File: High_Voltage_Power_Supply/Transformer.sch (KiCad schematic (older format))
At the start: 6 parts

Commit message: Finalised the schematic and BOM
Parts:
- TR1, TR2, TR3, TR4, TR5, TR6: renamed from TR?; Link (none) -> https://www.mouser.com/ProductDetail/Coilcraft/GA3460-BL?qs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
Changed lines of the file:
@@
 	3500 1800 3500 1700
 $Comp
-L High_Voltage_Power_Supply:GA3460-BL TR?
+L High_Voltage_Power_Supply:GA3460-BL TR1
 U 1 1 5F60E716
 P 4100 2000
-F 0 "TR?" H 4057 1285 50  0000 C CNN
+F 0 "TR1" H 4057 1285 50  0000 C CNN
 F 1 "GA3460-BL" H 4057 1376 50  0000 C CNN
 F 2 "High_Voltage_Power_Supply:Transformer_Coilcraft_GA3460-BL" H 4150 1300 50  0001 C CNN
-F 3 "" H 4000 2000 50  0001 C CNN
+F 3 "https://www.mouser.com/datasheet/2/597/ga3459-463457.pdf" H 4000 2000 50  0001 C CNN
+F 4 "https://www.mouser.com/ProductDetail/Coilcraft/GA3460-BL?qs=ZYnrCdKdyeeqpRItZMyzHA%3D%3D" H 4100 2000 50  0001 C CNN "Link"
 	1    4100 2000
 	1    0    0    1
 $EndComp
 $Comp
-L High_Voltage_Power_Supply:GA3460-BL TR?
+L High_Voltage_Power_Supply:GA3460-BL TR2
 U 1 1 5F683ED0
 P 6600 2000
-F 0 "TR?" H 6557 1285 50  0000 C CNN
+F 0 "TR2" H 6557 1285 50  0000 C CNN
 F 1 "GA3460-BL" H 6557 1376 50  0000 C CNN
 F 2 "High_Voltage_Power_Supply:Transformer_Coilcraft_GA3460-BL" H 6650 1300 50  0001 C CNN
-F 3 "" H 6500 2000 50  0001 C CNN
+F 3 "https://www.mouser.com/datasheet/2/597/ga3459-463457.pdf" H 6500 2000 50  0001 C CNN
+F 4 "https://www.mouser.com/ProductDetail/Coilcraft/GA3460-BL?qs=ZYnrCdKdyeeqpRItZMyzHA%3D%3D" H 6600 2000 50  0001 C CNN "Link"
 	1    6600 2000
 	1    0    0    1
@@
 	6000 2500 6000 2600
 $Comp
-L High_Voltage_Power_Supply:GA3460-BL TR?
+L High_Voltage_Power_Supply:GA3460-BL TR3
 U 1 1 5F68609E
 P 4100 3500
-F 0 "TR?" H 4057 2785 50  0000 C CNN
+F 0 "TR3" H 4057 2785 50  0000 C CNN
 F 1 "GA3460-BL" H 4057 2876 50  0000 C CNN
 F 2 "High_Voltage_Power_Supply:Transformer_Coilcraft_GA3460-BL" H 4150 2800 50  0001 C CNN
-F 3 "" H 4000 3500 50  0001 C CNN
+F 3 "https://www.mouser.com/datasheet/2/597/ga3459-463457.pdf" H 4000 3500 50  0001 C CNN
+F 4 "https://www.mouser.com/ProductDetail/Coilcraft/GA3460-BL?qs=ZYnrCdKdyeeqpRItZMyzHA%3D%3D" H 4100 3500 50  0001 C CNN "Link"
 	1    4100 3500
 	1    0    0    1
@@
 	3500 4000 3500 4100
 $Comp
-L High_Voltage_Power_Supply:GA3460-BL TR?
+L High_Voltage_Power_Supply:GA3460-BL TR4
 U 1 1 5F6896C3
 P 6600 3500
-F 0 "TR?" H 6557 2785 50  0000 C CNN
+F 0 "TR4" H 6557 2785 50  0000 C CNN
 F 1 "GA3460-BL" H 6557 2876 50  0000 C CNN
 F 2 "High_Voltage_Power_Supply:Transformer_Coilcraft_GA3460-BL" H 6650 2800 50  0001 C CNN
-F 3 "" H 6500 3500 50  0001 C CNN
+F 3 "https://www.mouser.com/datasheet/2/597/ga3459-463457.pdf" H 6500 3500 50  0001 C CNN
+F 4 "https://www.mouser.com/ProductDetail/Coilcraft/GA3460-BL?qs=ZYnrCdKdyeeqpRItZMyzHA%3D%3D" H 6600 3500 50  0001 C CNN "Link"
 	1    6600 3500
 	1    0    0    1
@@
 	6000 4000 6000 4100
 $Comp
-L High_Voltage_Power_Supply:GA3460-BL TR?
+L High_Voltage_Power_Supply:GA3460-BL TR6
 U 1 1 5F68DCC8
 P 6600 5000
-F 0 "TR?" H 6557 4285 50  0000 C CNN
+F 0 "TR6" H 6557 4285 50  0000 C CNN
 F 1 "GA3460-BL" H 6557 4376 50  0000 C CNN
 F 2 "High_Voltage_Power_Supply:Transformer_Coilcraft_GA3460-BL" H 6650 4300 50  0001 C CNN
-F 3 "" H 6500 5000 50  0001 C CNN
+F 3 "https://www.mouser.com/datasheet/2/597/ga3459-463457.pdf" H 6500 5000 50  0001 C CNN
+F 4 "https://www.mouser.com/ProductDetail/Coilcraft/GA3460-BL?qs=ZYnrCdKdyeeqpRItZMyzHA%3D%3D" H 6600 5000 50  0001 C CNN "Link"
 	1    6600 5000
 	1    0    0    1
 $EndComp
 $Comp
-L High_Voltage_Power_Supply:GA3460-BL TR?
+L High_Voltage_Power_Supply:GA3460-BL TR5
 U 1 1 5F69028C
 P 4100 5000
-F 0 "TR?" H 4057 4285 50  0000 C CNN
+F 0 "TR5" H 4057 4285 50  0000 C CNN
 F 1 "GA3460-BL" H 4057 4376 50  0000 C CNN
 F 2 "High_Voltage_Power_Supply:Transformer_Coilcraft_GA3460-BL" H 4150 4300 50  0001 C CNN
-F 3 "" H 4000 5000 50  0001 C CNN
+F 3 "https://www.mouser.com/datasheet/2/597/ga3459-463457.pdf" H 4000 5000 50  0001 C CNN
+F 4 "https://www.mouser.com/ProductDetail/Coilcraft/GA3460-BL?qs=ZYnrCdKdyeeqpRItZMyzHA%3D%3D" H 4100 5000 50  0001 C CNN "Link"
 	1    4100 5000
 	1    0    0    1

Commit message: Finished most of the PCB layout
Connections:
- net in+: now also TR2.1, TR2.2, TR2.3, TR2.4; no longer TR2.10, TR2.11, TR2.12, TR2.9
- net in-: now also TR6.10, TR6.11, TR6.12, TR6.9; no longer TR6.1, TR6.2, TR6.3, TR6.4
- net out+: now also TR2.6; no longer TR2.7
- net out-: now also TR6.7; no longer TR6.6
- net at TR1.1, TR1.2, TR1.3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: now also TR2.10, TR2.11, TR2.12, TR2.9, TR4.1, TR4.2, TR4.3, TR4.4; no longer TR2.1, TR2.2, TR2.3, TR2.4, TR4.10, TR4.11, TR4.12, TR4.9
- net at TR1.6, TR3.7: now also TR2.7, TR4.6; no longer TR2.6, TR4.7
- net at TR3.1, TR3.2, TR3.3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: now also TR4.10, TR4.11, TR4.12, TR4.9, TR6.1, TR6.2, TR6.3, TR6.4; no longer TR4.1, TR4.2, TR4.3, TR4.4, TR6.10, TR6.11, TR6.12, TR6.9
- net at TR3.6, TR5.7: now also TR4.7, TR6.6; no longer TR4.6, TR6.7
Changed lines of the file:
@@
 F 4 "https://www.mouser.com/ProductDetail/Coilcraft/GA3460-BL?qs=ZYnrCdKdyeeqpRItZMyzHA%3D%3D" H 6600 2000 50  0001 C CNN "Link"
 	1    6600 2000
-	1    0    0    1
+	1    0    0    -1
 $EndComp
 Wire Wire Line
@@
 F 4 "https://www.mouser.com/ProductDetail/Coilcraft/GA3460-BL?qs=ZYnrCdKdyeeqpRItZMyzHA%3D%3D" H 6600 3500 50  0001 C CNN "Link"
 	1    6600 3500
-	1    0    0    1
+	1    0    0    -1
 $EndComp
 Wire Wire Line
@@
 F 4 "https://www.mouser.com/ProductDetail/Coilcraft/GA3460-BL?qs=ZYnrCdKdyeeqpRItZMyzHA%3D%3D" H 6600 5000 50  0001 C CNN "Link"
 	1    6600 5000
-	1    0    0    1
+	1    0    0    -1
 $EndComp
 $Comp

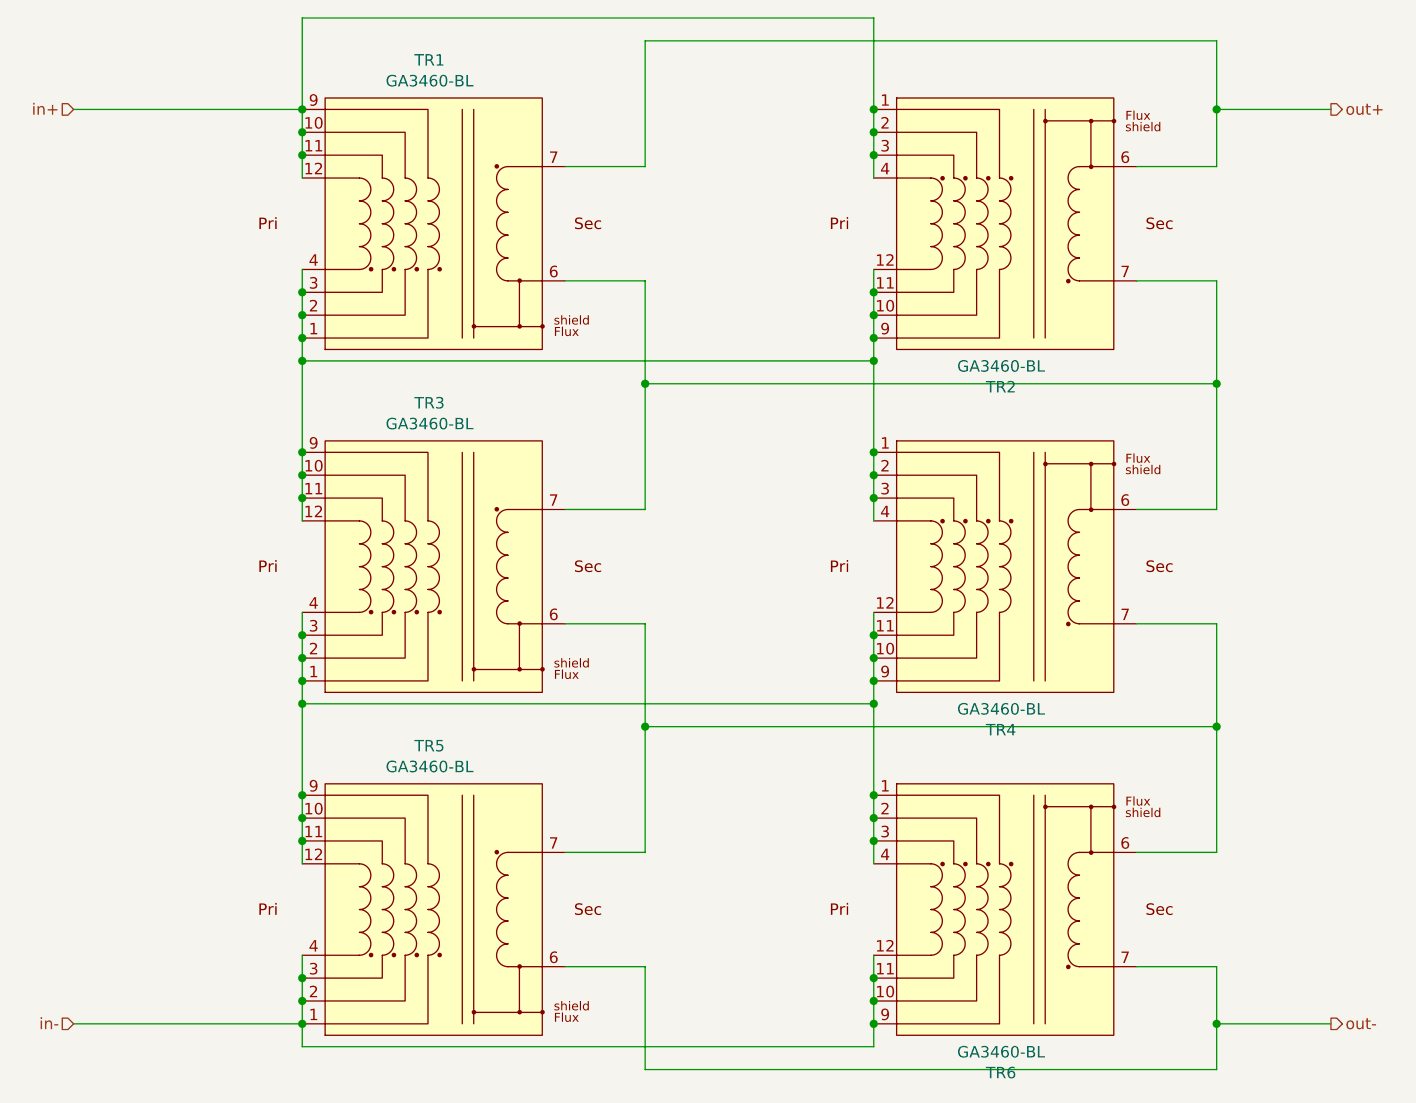
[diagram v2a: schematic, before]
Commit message: Updated schematic to run on regulation mode only
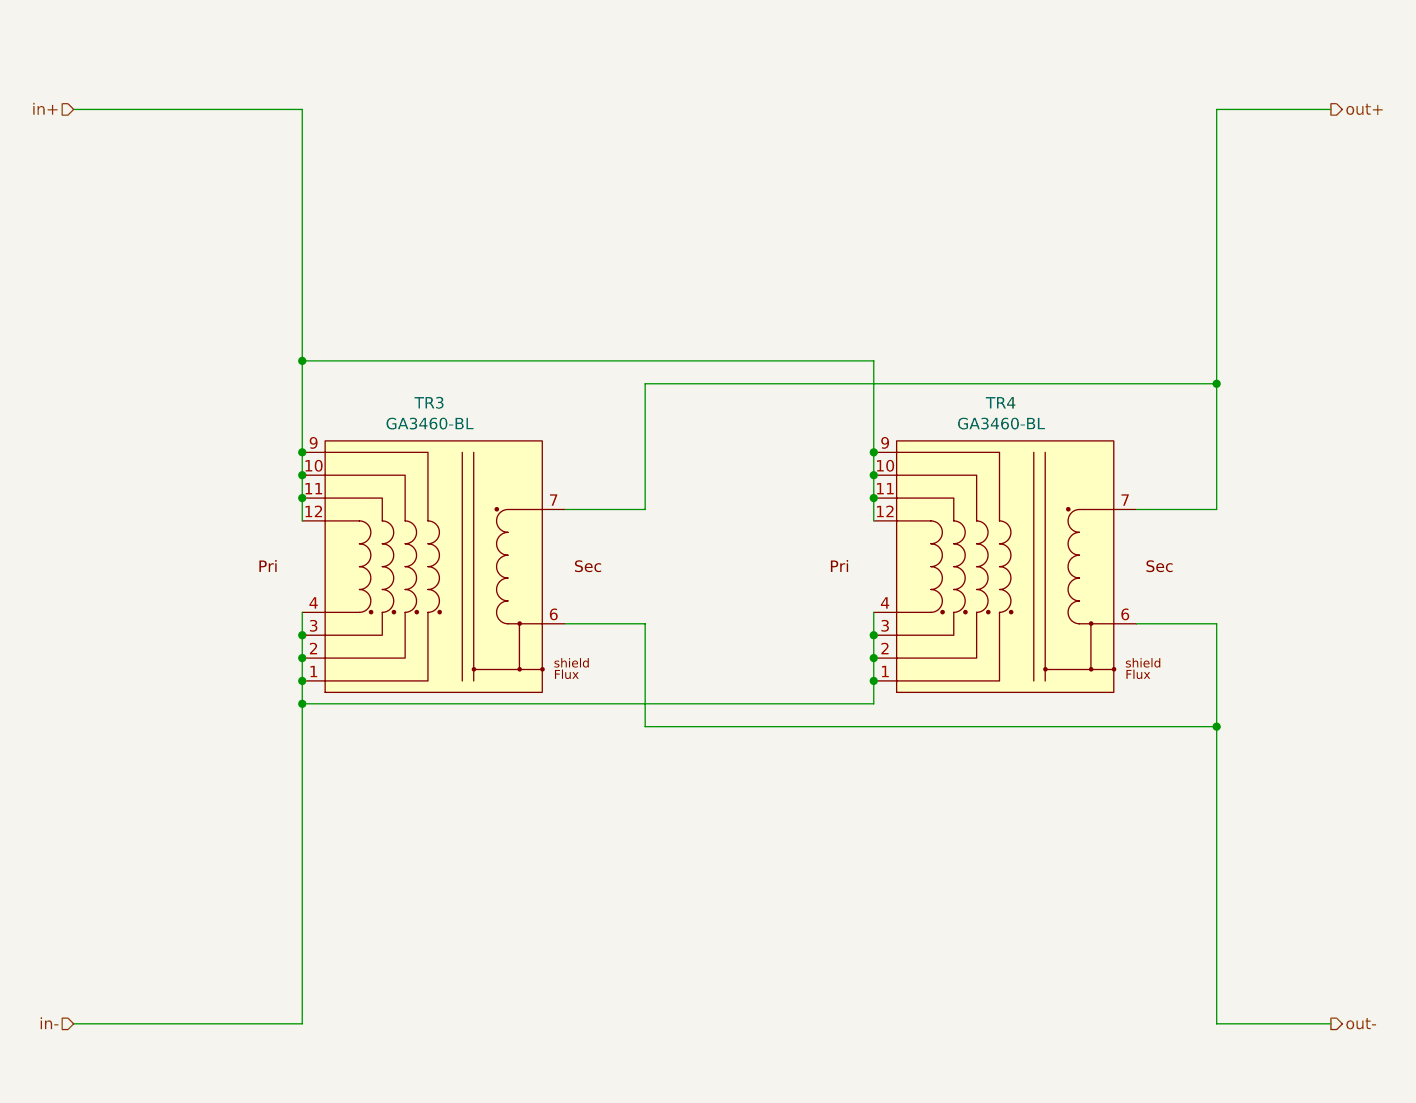
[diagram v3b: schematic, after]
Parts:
- removed TR1, TR2, TR5, TR6: GA3460-BL, High_Voltage_Power_Supply:Transformer_Coilcraft_GA3460-BL, symbol High_Voltage_Power_Supply:GA3460-BL
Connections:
- net in+: now also TR3.10, TR3.11, TR3.12, TR3.9, TR4.10, TR4.11, TR4.12, TR4.9
- net in-: now also TR3.1, TR3.2, TR3.3, TR3.4, TR4.1, TR4.2, TR4.3, TR4.4
- net out+: now also TR3.7, TR4.7
- net out-: now also TR3.6, TR4.6
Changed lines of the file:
@@
 	2500 5500 3500 5500
 Wire Wire Line
-	3500 2600 6000 2600
-Wire Wire Line
 	3500 4100 6000 4100
-Connection ~ 6000 4100
-Connection ~ 3500 4100
-Connection ~ 3500 2600
-Connection ~ 6000 2600
 Wire Wire Line
 	2500 1500 3500 1500
-Connection ~ 3500 1500
 Wire Wire Line
 	4650 3250 5000 3250
@@
 	5000 3250 5000 2700
 Wire Wire Line
-	4650 4750 5000 4750
-Wire Wire Line
-	5000 4750 5000 4200
-Wire Wire Line
 	4650 3750 5000 3750
 Wire Wire Line
 	5000 3750 5000 4200
-Connection ~ 5000 4200
-Wire Wire Line
-	4650 2250 5000 2250
-Wire Wire Line
-	5000 2250 5000 2700
-Connection ~ 5000 2700
-Wire Wire Line
-	4650 1750 5000 1750
-Wire Wire Line
-	5000 1750 5000 1200
-Wire Wire Line
-	5000 1200 7500 1200
-Wire Wire Line
-	7150 1750 7500 1750
-Wire Wire Line
-	7500 1750 7500 1500
 Wire Wire Line
 	7500 3250 7500 2700
 Wire Wire Line
-	7500 2250 7150 2250
-Wire Wire Line
 	5000 2700 7500 2700
 Connection ~ 7500 2700
-Wire Wire Line
-	7500 2700 7500 2250
 Wire Wire Line
 	7150 3250 7500 3250
@@
 	7500 3750 7500 4200
 Wire Wire Line
-	7500 4750 7150 4750
-Wire Wire Line
 	5000 4200 7500 4200
 Connection ~ 7500 4200
 Wire Wire Line
-	7500 4200 7500 4750
-Wire Wire Line
-	4650 5250 5000 5250
-Wire Wire Line
-	5000 5250 5000 5700
-Wire Wire Line
-	5000 5700 7500 5700
-Wire Wire Line
-	7500 5700 7500 5500
-Wire Wire Line
-	7500 5250 7150 5250
-Wire Wire Line
 	8000 5500 7500 5500
-Connection ~ 7500 5500
-Wire Wire Line
-	7500 5500 7500 5250
 Wire Wire Line
 	7500 1500 8000 1500
-Connection ~ 7500 1500
-Wire Wire Line
-	7500 1500 7500 1200
-Wire Wire Line
-	3500 1500 3500 1100
-Wire Wire Line
-	3500 1100 6000 1100
-Wire Wire Line
-	3500 4100 3500 4500
-Wire Wire Line
-	3500 2600 3500 3000
-Wire Wire Line
-	6000 2600 6000 3000
-Connection ~ 3500 2500
-Wire Wire Line
-	3500 2500 3500 2600
-Connection ~ 3500 2400
-Wire Wire Line
-	3500 2300 3500 2200
-Connection ~ 3500 2300
-Wire Wire Line
-	3500 2400 3500 2300
-Wire Wire Line
-	3500 2500 3500 2400
-Connection ~ 3500 1700
-Wire Wire Line
-	3500 1600 3500 1500
-Connection ~ 3500 1600
-Wire Wire Line
-	3500 1700 3500 1600
-Wire Wire Line
-	3500 1800 3500 1700
-$Comp
-L High_Voltage_Power_Supply:GA3460-BL TR1
-U 1 1 5F60E716
-P 4100 2000
-F 0 "TR1" H 4057 1285 50  0000 C CNN
-F 1 "GA3460-BL" H 4057 1376 50  0000 C CNN
-F 2 "High_Voltage_Power_Supply:Transformer_Coilcraft_GA3460-BL" H 4150 1300 50  0001 C CNN
-F 3 "https://www.mouser.com/datasheet/2/597/ga3459-463457.pdf" H 4000 2000 50  0001 C CNN
-F 4 "https://www.mouser.com/ProductDetail/Coilcraft/GA3460-BL?qs=ZYnrCdKdyeeqpRItZMyzHA%3D%3D" H 4100 2000 50  0001 C CNN "Link"
-	1    4100 2000
-	1    0    0    1
-$EndComp
-$Comp
-L High_Voltage_Power_Supply:GA3460-BL TR2
-U 1 1 5F683ED0
-P 6600 2000
-F 0 "TR2" H 6557 1285 50  0000 C CNN
-F 1 "GA3460-BL" H 6557 1376 50  0000 C CNN
-F 2 "High_Voltage_Power_Supply:Transformer_Coilcraft_GA3460-BL" H 6650 1300 50  0001 C CNN
-F 3 "https://www.mouser.com/datasheet/2/597/ga3459-463457.pdf" H 6500 2000 50  0001 C CNN
-F 4 "https://www.mouser.com/ProductDetail/Coilcraft/GA3460-BL?qs=ZYnrCdKdyeeqpRItZMyzHA%3D%3D" H 6600 2000 50  0001 C CNN "Link"
-	1    6600 2000
-	1    0    0    -1
-$EndComp
-Wire Wire Line
-	6000 2500 6000 2600
 $Comp
 L High_Voltage_Power_Supply:GA3460-BL TR3
@@
 F 4 "https://www.mouser.com/ProductDetail/Coilcraft/GA3460-BL?qs=ZYnrCdKdyeeqpRItZMyzHA%3D%3D" H 6600 3500 50  0001 C CNN "Link"
 	1    6600 3500
-	1    0    0    -1
+	1    0    0    1
 $EndComp
 Wire Wire Line
 	6000 4000 6000 4100
-$Comp
-L High_Voltage_Power_Supply:GA3460-BL TR6
-U 1 1 5F68DCC8
-P 6600 5000
-F 0 "TR6" H 6557 4285 50  0000 C CNN
-F 1 "GA3460-BL" H 6557 4376 50  0000 C CNN
-F 2 "High_Voltage_Power_Supply:Transformer_Coilcraft_GA3460-BL" H 6650 4300 50  0001 C CNN
-F 3 "https://www.mouser.com/datasheet/2/597/ga3459-463457.pdf" H 6500 5000 50  0001 C CNN
-F 4 "https://www.mouser.com/ProductDetail/Coilcraft/GA3460-BL?qs=ZYnrCdKdyeeqpRItZMyzHA%3D%3D" H 6600 5000 50  0001 C CNN "Link"
-	1    6600 5000
-	1    0    0    -1
-$EndComp
-$Comp
-L High_Voltage_Power_Supply:GA3460-BL TR5
-U 1 1 5F69028C
-P 4100 5000
-F 0 "TR5" H 4057 4285 50  0000 C CNN
-F 1 "GA3460-BL" H 4057 4376 50  0000 C CNN
-F 2 "High_Voltage_Power_Supply:Transformer_Coilcraft_GA3460-BL" H 4150 4300 50  0001 C CNN
-F 3 "https://www.mouser.com/datasheet/2/597/ga3459-463457.pdf" H 4000 5000 50  0001 C CNN
-F 4 "https://www.mouser.com/ProductDetail/Coilcraft/GA3460-BL?qs=ZYnrCdKdyeeqpRItZMyzHA%3D%3D" H 4100 5000 50  0001 C CNN "Link"
-	1    4100 5000
-	1    0    0    1
-$EndComp
-Wire Wire Line
-	3500 5200 3500 5300
-Connection ~ 3500 5500
-Connection ~ 3500 5300
-Wire Wire Line
-	3500 5300 3500 5400
-Connection ~ 3500 5400
-Wire Wire Line
-	3500 5400 3500 5500
-Wire Wire Line
-	3500 4500 3500 4600
-Connection ~ 3500 4500
-Connection ~ 3500 4600
-Wire Wire Line
-	3500 4600 3500 4700
-Connection ~ 3500 4700
-Wire Wire Line
-	3500 4700 3500 4800
 Wire Wire Line
 	3500 3700 3500 3800
@@
 	3500 3200 3500 3300
 Wire Wire Line
-	6000 2200 6000 2300
-Connection ~ 6000 2500
-Connection ~ 6000 2300
-Wire Wire Line
-	6000 2300 6000 2400
-Connection ~ 6000 2400
-Wire Wire Line
-	6000 2400 6000 2500
-Wire Wire Line
-	6000 1100 6000 1500
-Connection ~ 6000 1500
-Wire Wire Line
-	6000 1500 6000 1600
-Connection ~ 6000 1600
-Wire Wire Line
-	6000 1600 6000 1700
-Connection ~ 6000 1700
-Wire Wire Line
-	6000 1700 6000 1800
-Wire Wire Line
 	6000 3000 6000 3100
-Connection ~ 6000 3000
 Connection ~ 6000 3100
 Wire Wire Line
@@
 	6000 3900 6000 4000
 Wire Wire Line
-	6000 5200 6000 5300
-Connection ~ 6000 5300
+	7500 4200 7500 5500
 Wire Wire Line
-	6000 5300 6000 5400
-Connection ~ 6000 5400
+	3500 4100 3500 5500
+Connection ~ 3500 4100
 Wire Wire Line
-	6000 5400 6000 5500
+	7500 1500 7500 2700
 Wire Wire Line
-	6000 4100 6000 4500
-Connection ~ 6000 4500
+	3500 1500 3500 2600
 Wire Wire Line
-	6000 4500 6000 4600
-Connection ~ 6000 4600
+	3500 2600 3500 3000
+Connection ~ 3500 2600
 Wire Wire Line
-	6000 4600 6000 4700
-Connection ~ 6000 4700
+	3500 2600 6000 2600
+Connection ~ 6000 3000
 Wire Wire Line
-	6000 4700 6000 4800
-Wire Wire Line
-	3500 5500 3500 5600
-Wire Wire Line
-	3500 5600 6000 5600
-Wire Wire Line
-	6000 5600 6000 5500
-Connection ~ 6000 5500
+	6000 2600 6000 3000
 $EndSCHEMATC

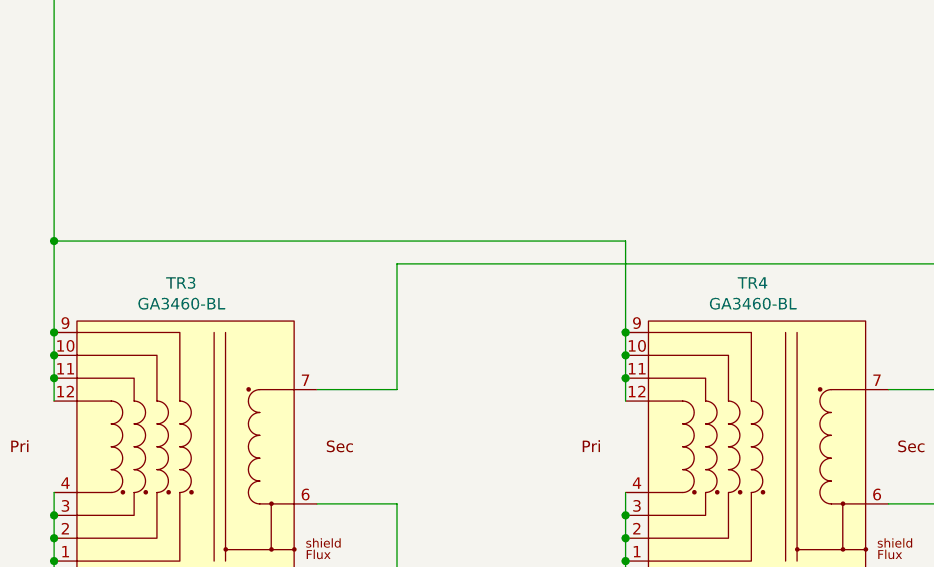
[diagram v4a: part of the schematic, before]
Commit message: Finished the v2 of the schematic
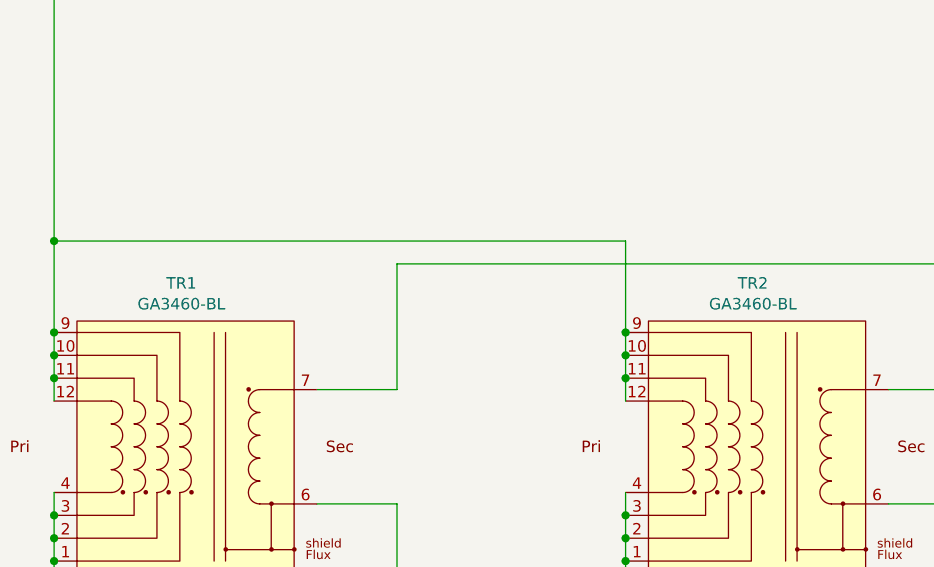
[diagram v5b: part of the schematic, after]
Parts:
- renumbered TR3 to TR1, TR4 to TR2
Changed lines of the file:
@@
 	7500 1500 8000 1500
 $Comp
-L High_Voltage_Power_Supply:GA3460-BL TR3
+L High_Voltage_Power_Supply:GA3460-BL TR1
 U 1 1 5F68609E
 P 4100 3500
-AR Path="/5F5CFB04/5F68609E" Ref="TR3"  Part="1"
+AR Path="/5F5CFB04/5F68609E" Ref="TR1"  Part="1"
 AR Path="/5F8F508C/5F68609E" Ref="TR?"  Part="1"
-F 0 "TR3" H 4057 2785 50  0000 C CNN
+F 0 "TR1" H 4057 2785 50  0000 C CNN
 F 1 "GA3460-BL" H 4057 2876 50  0000 C CNN
 F 2 "High_Voltage_Power_Supply:Transformer_Coilcraft_GA3460-BL" H 4150 2800 50  0001 C CNN
@@
 Wire Wire Line
 	3500 4000 3500 4100
-$Comp
-L High_Voltage_Power_Supply:GA3460-BL TR4
-U 1 1 5F6896C3
-P 6600 3500
-AR Path="/5F5CFB04/5F6896C3" Ref="TR4"  Part="1"
-AR Path="/5F8F508C/5F6896C3" Ref="TR?"  Part="1"
-F 0 "TR4" H 6557 2785 50  0000 C CNN
-F 1 "GA3460-BL" H 6557 2876 50  0000 C CNN
-F 2 "High_Voltage_Power_Supply:Transformer_Coilcraft_GA3460-BL" H 6650 2800 50  0001 C CNN
-F 3 "https://www.mouser.com/datasheet/2/597/ga3459-463457.pdf" H 6500 3500 50  0001 C CNN
-F 4 "https://www.mouser.com/ProductDetail/Coilcraft/GA3460-BL?qs=ZYnrCdKdyeeqpRItZMyzHA%3D%3D" H 6600 3500 50  0001 C CNN "Link"
-	1    6600 3500
-	1    0    0    1
-$EndComp
 Wire Wire Line
 	6000 4000 6000 4100
@@
 Wire Wire Line
 	6000 2600 6000 3000
+$Comp
+L High_Voltage_Power_Supply:GA3460-BL TR2
+U 1 1 5F6896C3
+P 6600 3500
+AR Path="/5F5CFB04/5F6896C3" Ref="TR2"  Part="1"
+AR Path="/5F8F508C/5F6896C3" Ref="TR?"  Part="1"
+F 0 "TR2" H 6557 2785 50  0000 C CNN
+F 1 "GA3460-BL" H 6557 2876 50  0000 C CNN
+F 2 "High_Voltage_Power_Supply:Transformer_Coilcraft_GA3460-BL" H 6650 2800 50  0001 C CNN
+F 3 "https://www.mouser.com/datasheet/2/597/ga3459-463457.pdf" H 6500 3500 50  0001 C CNN
+F 4 "https://www.mouser.com/ProductDetail/Coilcraft/GA3460-BL?qs=ZYnrCdKdyeeqpRItZMyzHA%3D%3D" H 6600 3500 50  0001 C CNN "Link"
+	1    6600 3500
+	1    0    0    1
+$EndComp
 $EndSCHEMATC
